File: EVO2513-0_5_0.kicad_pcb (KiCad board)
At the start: 8 copper layers, 110 x 69 mm, 231 parts, among them J1 1053101204, J2 1053101114, J3 10144517-043802LF, J4 1053102204, J5 1053091102, J6 1053091102, M1 78614150960, M2 78614150960, M3 78614150960, M4 78614150960, M5 78614150960, M6 78614150960, Q1 DMT4011LFG, Q10 DMT4011LFG, Q11 DMT4011LFG, Q12 DMP3018SFV, Q13 DMP3018SFV, Q14 DMP3018SFV, Q15 DMP3018SFV, Q16 IAUCN04S7L019, Q17 IAUCN04S7L028, Q18 CSD17304Q3, Q19 IAUCN04S7L019, Q20 DMN65D8LFB-7, Q21 DMN65D8LFB-7, Q22 DMN65D8LFB-7, Q3 DMT4011LFG, Q4 DMP3018SFV, Q5 DMP3018SFV, Q6 DMT4011LFG, Q7 DMT4011LFG, Q8 DMT4011LFG, Q9 DMT4011LFG, U1 LTC1960, U10 TLV9002IDSG, U2 LTC4365, U5 LM51772RHAR, U6 TPS22811, U7 TPS22811, U8 TLV9002IDSG, U9 TPS22811

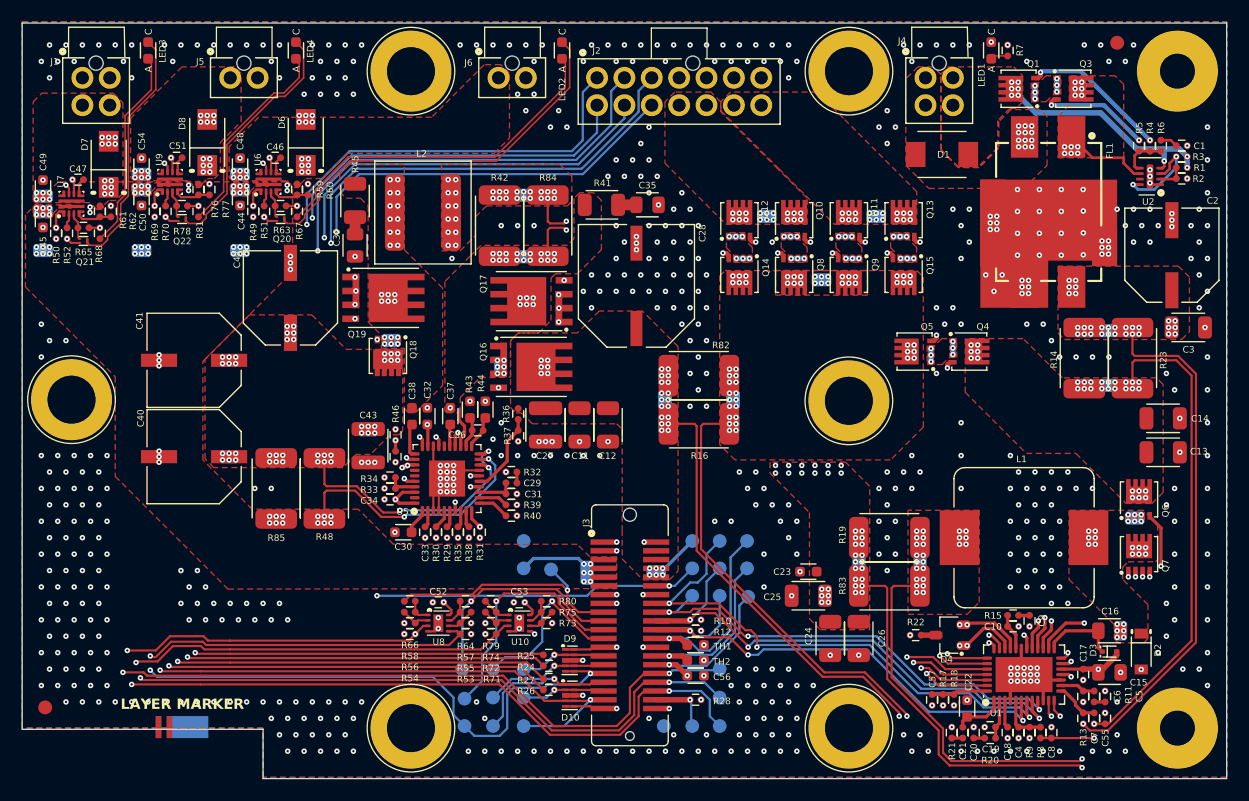
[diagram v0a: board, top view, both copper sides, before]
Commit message: Use KiCad standard footprints for chip resistors and capacitors
The imported Lattech R/C footprints have poor land patterns (the 0402s
use 0.635 mm circular pads) and cause tombstoning in assembly. Replace
all 139 chip resistors and capacitors with KiCad's standard IPC-7351
nominal footprints:

  Res 0402/0603/1206/2512 -> Resistor_SMD:R_xxxx_xxxxMetric (87)
  Cap 0402/0603/0805/1206/1210 -> Capacitor_SMD:C_xxxx_xxxxMetric (52)

Each part keeps its position, rotation, side, pad nets, schematic link
and reference/value text placement. The pads are on the same axis with
pad 1 on the same side, and every old pad centre lies inside the new
pad, so existing tracks still connect. Zones are refilled.

Schematic Footprint fields and the symbols' footprint filters point at
the new footprints, and the unused imported R/C footprints are removed
from the project library. Electrolytic capacitors are not changed.

DRC: 0 unconnected items, as before. Tracks, vias, zone outlines and
all other footprints are unchanged. 11 courtyard overlaps are new,
because the old footprints had no courtyards.

Co-Authored-By: Claude Opus 5.5 <noreply@anthropic.com>
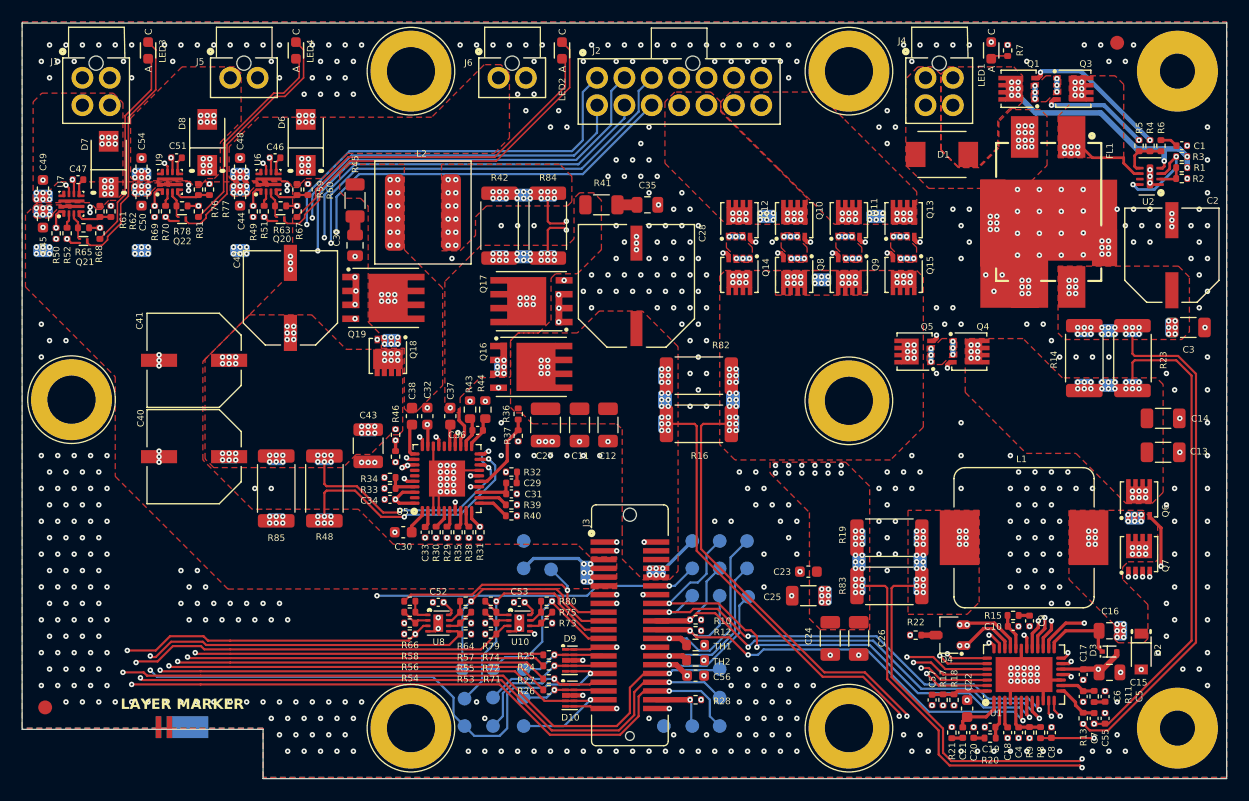
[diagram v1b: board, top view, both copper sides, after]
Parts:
- C1, C10, C17, C18, C19, C20, C21, C29, C31, C33, C34, C36, C4, C46, C47, C5, C51, C52, C53, C55, C57, C6, C7, C8, C9: footprint EVO2513-0_5_0-import-fps:Cap 0402 H0-6 R -> Capacitor_SMD:C_0402_1005Metric
- C11, C12, C13, C14, C24, C25, C26, C3: footprint EVO2513-0_5_0-import-fps:Cap 1206 H1-8 -> Capacitor_SMD:C_1206_3216Metric
- C15, C16, C35, C39: footprint EVO2513-0_5_0-import-fps:Cap 0805 H1-4 -> Capacitor_SMD:C_0805_2012Metric
- C22, C23, C30, C32, C37, C38, C44, C45, C48, C49, C50, C54, C56: footprint EVO2513-0_5_0-import-fps:Cap 0603 H0-9 -> Capacitor_SMD:C_0603_1608Metric
- C27, C43: footprint EVO2513-0_5_0-import-fps:Cap 1210 H2-1 -> Capacitor_SMD:C_1210_3225Metric
- R1, R10, R11, R12, R13, R15, R17, R18, R2, R20, R21, R22, R24, R25, R26, R27, R28, R29, R3, R30, R31, R32, R33, R34, R35, R36, R37, R38, R39, R4, R40, R46, R47, R49, R5, R50, R51, R52, R53, R54, R55, R56, R57, R58, R59, R6, R60, R61, R62, R63, R64, R65, R66, R67, R68, R69, R7, R70, R71, R72, R73, R74, R75, R76, R77, R78, R79, R8, R80, R81, R9: footprint EVO2513-0_5_0-import-fps:Res 0402 H0-45 R -> Resistor_SMD:R_0402_1005Metric
- R14, R16, R19, R23, R42, R48, R82, R83, R84, R85: footprint EVO2513-0_5_0-import-fps:Res 2512 H0-9 -> Resistor_SMD:R_2512_6332Metric
- R41, R45: footprint EVO2513-0_5_0-import-fps:Res 1206 H0-55 -> Resistor_SMD:R_1206_3216Metric
- R43, R44, TH1, TH2: footprint EVO2513-0_5_0-import-fps:Res 0603 H0-45 -> Resistor_SMD:R_0603_1608Metric
